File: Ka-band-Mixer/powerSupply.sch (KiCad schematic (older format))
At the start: 33 parts, among them J1 Conn_01x02_Male, J2 Conn_01x02_Male, U2 LT1962-3.3, U3 LT3010, U5 LT1962-5, U6 LT1962-5

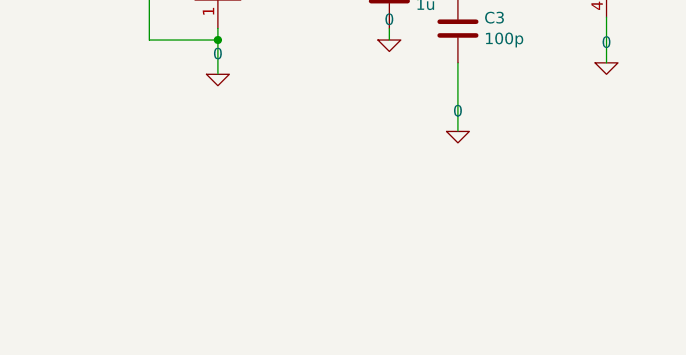
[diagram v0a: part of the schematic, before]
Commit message: ADD GND test probe
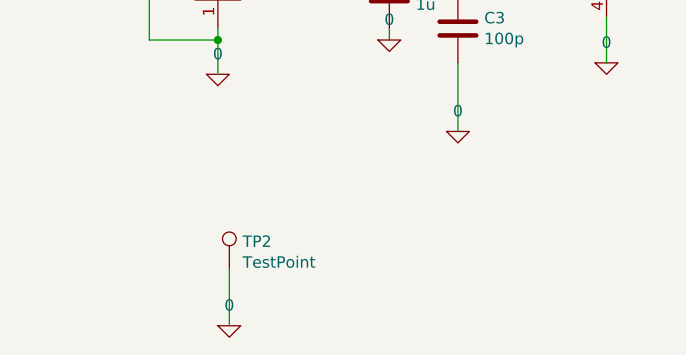
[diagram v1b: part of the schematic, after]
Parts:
- added TP2: TestPoint, TestPoint:TestPoint_Loop_D2.60mm_Drill1.6mm_Beaded, symbol frequencySynthesizer-rescue:TestPoint-frequencySintesizer
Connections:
- net 0: now also TP2.1
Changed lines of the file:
@@
 Wire Wire Line
 	6300 2050 6300 2300
+$Comp
+L pspice:0 #GND?
+U 1 1 5FCEB8DB
+P 1600 5450
+AR Path="/5FBD30A7/5FBFBF42/5FCEB8DB" Ref="#GND?"  Part="1"
+AR Path="/5FBD5B32/5FCEB8DB" Ref="#GND0138"  Part="1"
+F 0 "#GND0138" H 1600 5350 50  0001 C CNN
+F 1 "0" H 1600 5539 50  0000 C CNN
+F 2 "" H 1600 5450 50  0001 C CNN
+F 3 "~" H 1600 5450 50  0001 C CNN
+	1    1600 5450
+	1    0    0    -1
+$EndComp
+$Comp
+L frequencySynthesizer-rescue:TestPoint-frequencySintesizer TP?
+U 1 1 5FCF00F0
+P 1600 5200
+AR Path="/5FBD30A7/5FCF00F0" Ref="TP?"  Part="1"
+AR Path="/5FBD5B32/5FCF00F0" Ref="TP2"  Part="1"
+F 0 "TP2" H 1658 5318 50  0000 L CNN
+F 1 "TestPoint" H 1658 5227 50  0000 L CNN
+F 2 "TestPoint:TestPoint_Loop_D2.60mm_Drill1.6mm_Beaded" H 1800 5200 50  0001 C CNN
+F 3 "https://www.mouser.it/datasheet/2/215/005-5009-741293.pdf" H 1800 5200 50  0001 C CNN
+F 4 "5007" H 1600 5200 50  0001 C CNN "Manufacturer/Part Number"
+F 5 "Mouser 534-5007" H 1600 5200 50  0001 C CNN "Supplier Stock Code"
+	1    1600 5200
+	1    0    0    -1
+$EndComp
+Wire Wire Line
+	1600 5200 1600 5450
 $EndSCHEMATC
